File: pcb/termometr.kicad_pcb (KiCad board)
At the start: 2 copper layers, 100 parts, among them P1 CONN_01X03, P2 CONN_01X03, P3 CONN_01X02, Q1 MMBT2222ALT1G, Q10 MMBT2222ALT1G, Q11 MMBT2222ALT1G, Q12 FDV304P, Q13 FDV304P, Q14 MMBT2222ALT1G, Q15 MMBT2222ALT1G, Q16 MMBT2222ALT1G, Q17 MMBT2222ALT1G, Q2 MMBT2222ALT1G, Q3 MMBT2222ALT1G, Q4 MMBT2222ALT1G, Q5 FDV304P, Q6 MMBT2222ALT1G, Q7 FDV304P, Q8 FDV304P, Q9 FDV304P, U1 LT1009, U10 LM1117, U11 HEF4544B, U2 MCP6031, U3 PT100, U4 MCP6N16, U5 MCP3421A0T-E/CH, U6 STM32M030F4, U7 HEF4544B, U8 3x8, U9 3x8

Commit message: Next version. First iteration.
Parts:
- C12, C13, C14, C4, C5, C8, C9, Q1, Q10, Q14, Q15, Q16, Q17, Q2, Q3, Q6, R13, R14, R16, R20, R22, R26, R27, R28, R29, R3, R35, R36, R37, R47, R5, U6: moved to F.Cu
- U8, U9: footprint Displays_7-Segment:Cx56-12 -> footprint:3x7segment
- moved R1 243.1 mm to (30.8, 52.5), turned to 90 degrees
- moved R34 235.4 mm to (43.4, 55.5)
- moved C12 235.2 mm to (43.6, 48.5), turned to 90 degrees
- moved RV1 235.2 mm to (35.0, 53.7), turned to 0 degrees
- moved C13 231.6 mm to (32.2, 48.4), turned to 270 degrees
- moved C9 231.0 mm to (47.9, 48.3), turned to 0 degrees
- moved C8 230.4 mm to (46.9, 54.3), turned to 180 degrees
- moved U1 228.5 mm to (39.5, 52.9), turned to 270 degrees
- moved U5 227.6 mm to (47.0, 51.6), turned to 180 degrees
- moved R17 225.5 mm to (37.5, 48.8), turned to 180 degrees
- moved P3 220.8 mm to (31.4, 89.6), turned to 180 degrees
- moved R11 215.9 mm to (36.8, 85.8), turned to 0 degrees
- moved C4 211.9 mm to (37.7, 38.4), turned to 90 degrees
- moved R10 211.7 mm to (36.8, 88.4), turned to 0 degrees
- moved R18 209.9 mm to (53.8, 47.1)
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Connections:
- U6 pad 10: /S2 -> Net-(R22-Pad1)
- U6 pad 7: Net-(R22-Pad1) -> /S2
- U6 pad 8: Net-(R20-Pad1) -> /S3
- U6 pad 9: /S3 -> Net-(R20-Pad1)
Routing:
- net GND: track 844.8 -> 494.5 mm, vias 4 -> 7
- net Net-(Q1-Pad1): track 155.5 -> 15.0 mm
- net Net-(Q2-Pad1): track 139.1 -> 12.5 mm
- net Net-(Q3-Pad1): track 111.4 -> 9.96 mm
- net VCC: track 444.3 -> 358.6 mm
- net Net-(R20-Pad1): track 57.5 -> 7.41 mm
- net /S1: track 55.9 -> 6.23 mm
- net Net-(R19-Pad1): track 60.0 -> 12.0 mm, vias 0 -> 1
- net /S2: track 53.3 -> 9.39 mm
- net /S3: track 57.2 -> 13.3 mm
- net Net-(Q7-Pad3): track 43.6 -> 3.85 mm
- net Net-(Q5-Pad3): track 40.0 -> 3.75 mm, vias 2 -> 0
- net Net-(Q6-Pad1): track 44.2 -> 7.89 mm
- net Net-(Q12-Pad1): track 19.4 -> 55.5 mm, vias 0 -> 4
- net Net-(Q13-Pad3): track 38.8 -> 3.72 mm, vias 2 -> 0
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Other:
- net class Default: trace_width 0.25 -> 0.35
- net class Normal: clearance 0.4 -> 0.3
- net class Self' added: clearance 0.3, trace_width 0.7, via_dia 0.6, via_drill 0.4

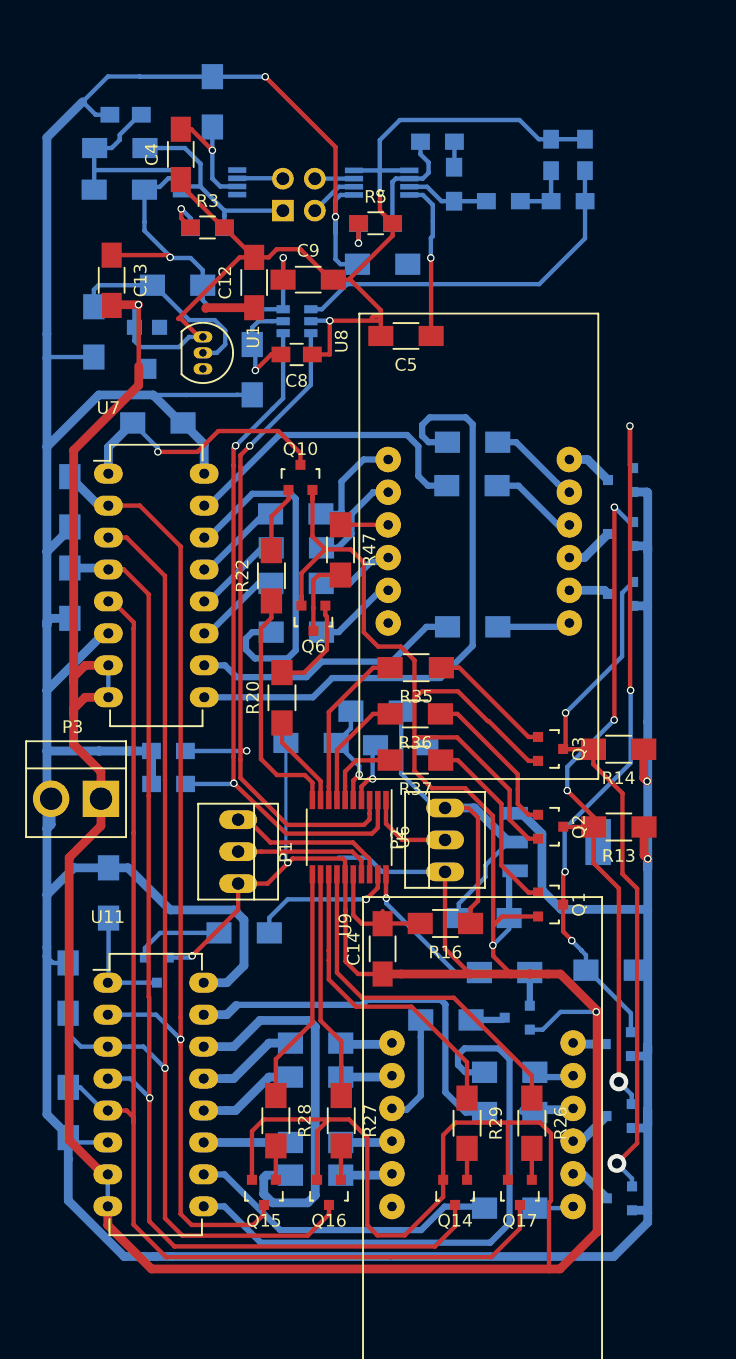
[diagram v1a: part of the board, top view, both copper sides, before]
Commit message: All connected with zones.
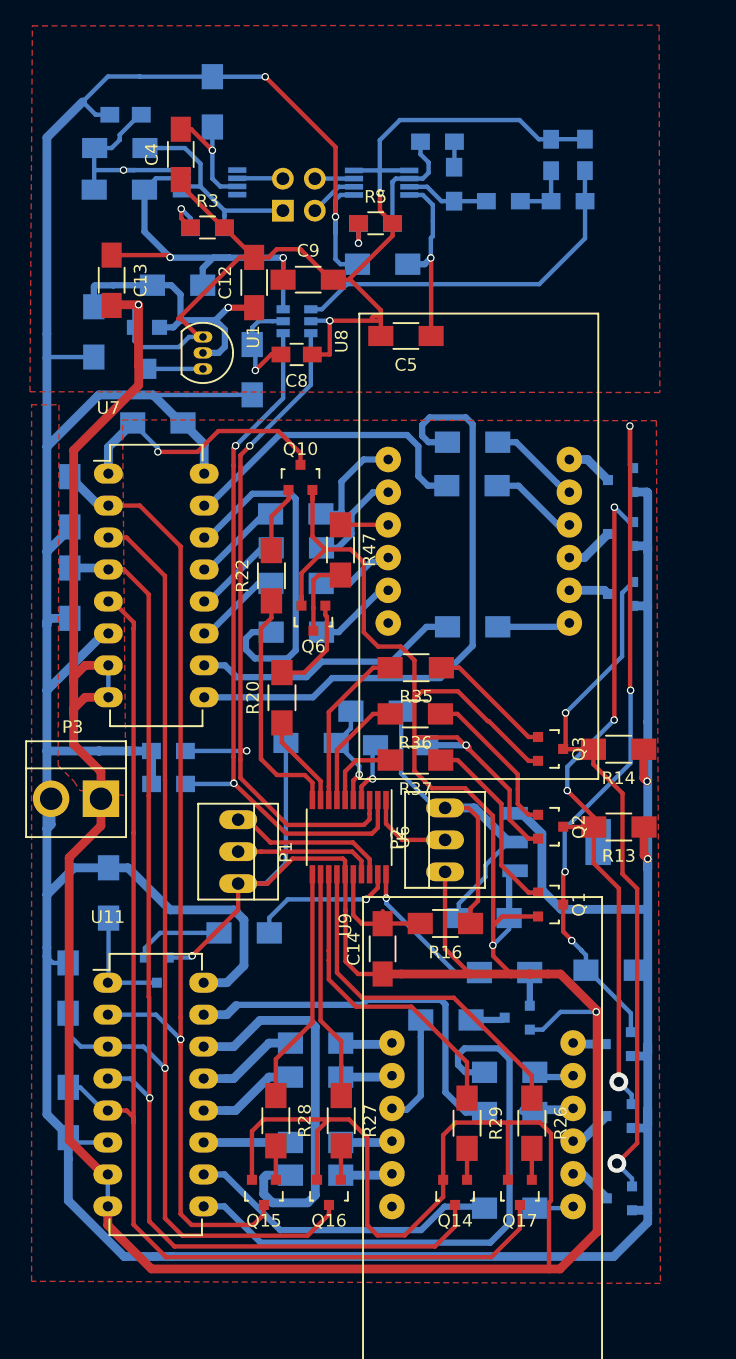
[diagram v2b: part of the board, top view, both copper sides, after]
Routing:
- net Net-(RV1-Pad2): track 0.00 -> 4.45 mm
- net Net-(C12-Pad1): track 20.5 -> 23.4 mm, vias 0 -> 1
- net Net-(C5-Pad1): track 12.7 -> 14.7 mm
- net 2V5: track 32.2 -> 33.0 mm
- net GND: vias 7 -> 8
- added copper zone on F.Cu, net GND
